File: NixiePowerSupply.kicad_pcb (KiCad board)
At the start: 2 copper layers, 50.8 x 44.4 mm, 21 parts, among them J1 BARREL_JACK, P1 CONN_01X03, P2 CONN_01X02, T1 IRF644, U1 MAX1771

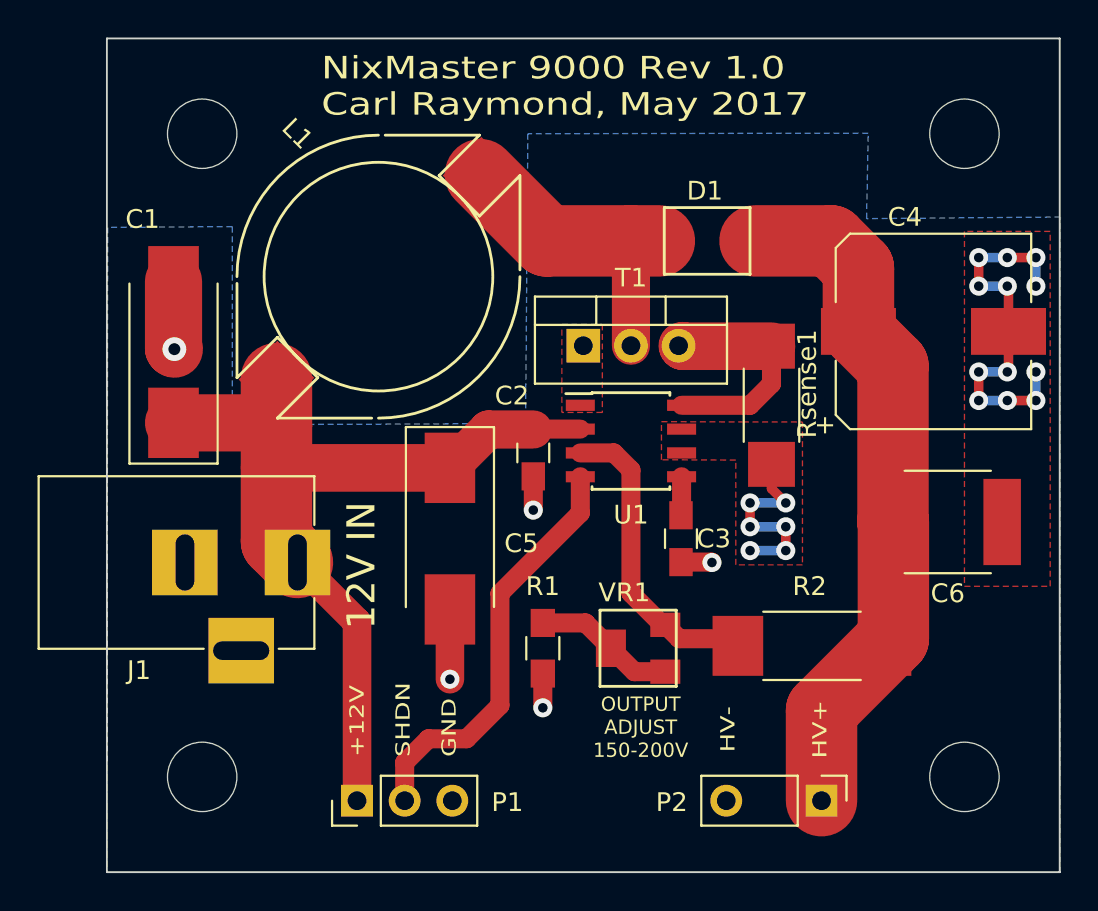
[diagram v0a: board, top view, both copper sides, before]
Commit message: Changed 12V jack to round-hole version
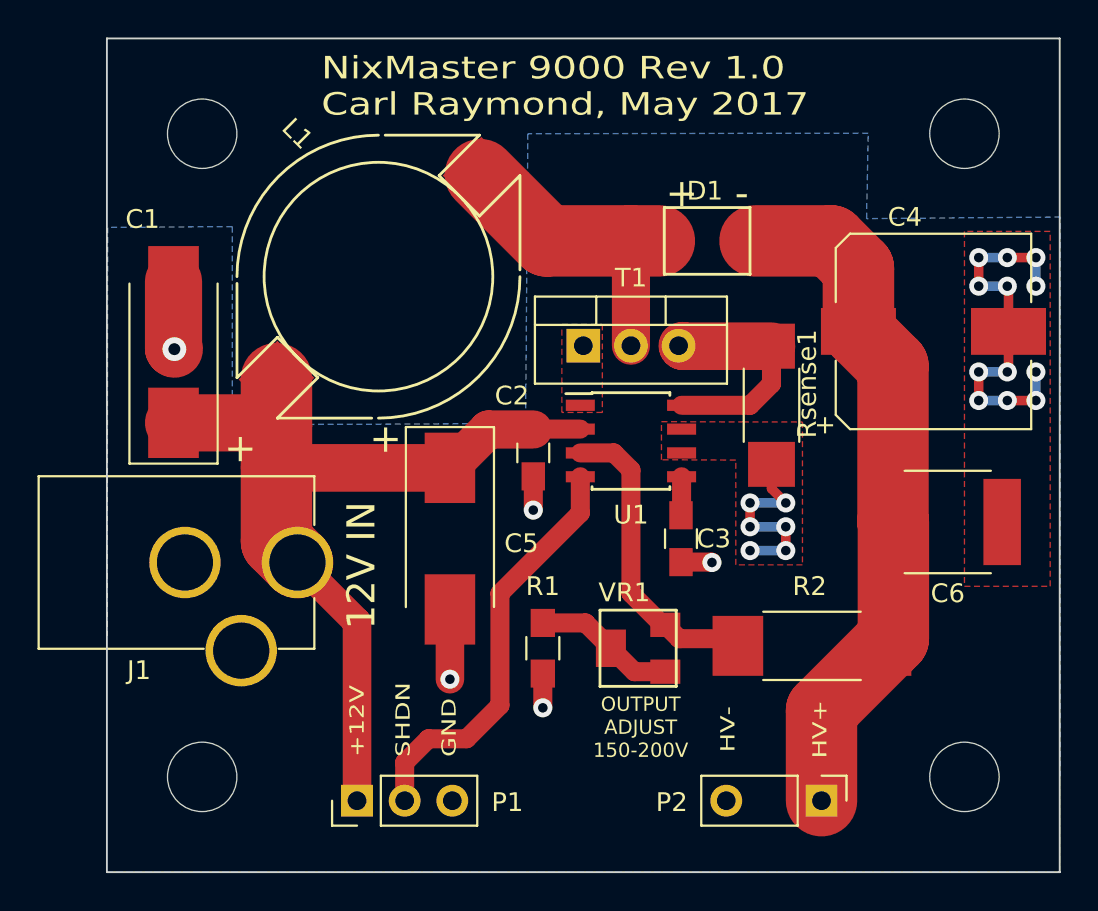
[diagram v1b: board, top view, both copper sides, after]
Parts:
- J1: footprint Connectors:BARREL_JACK -> nixie:BARREL_JACK_ROUND_HOLES
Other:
- board text added: "+"
- board text added: "+ -"
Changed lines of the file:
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@@
     (links 34)
     (no_connects 0)
-    (area 40.384999 24.805 99.568572 72.195)
+    (area 44.399999 25.349999 95.300001 69.900001)
     (thickness 1.6)
-    (drawings 9)
+    (drawings 12)
     (tracks 105)
     (zones 0)
@@
   )
   (setup
-    (last_trace_width 1.016)
+    (last_trace_width 0.25)
     (user_trace_width 0.508)
     (user_trace_width 1.016)
@@
     (visible_elements 7FFFFFFF)
     (pcbplotparams
-      (layerselection 0x010a0_00000001)
-      (usegerberextensions false)
+      (layerselection 0x010f0_80000001)
+      (usegerberextensions true)
       (excludeedgelayer true)
       (linewidth 0.100000)
@@
       (padsonsilk false)
       (subtractmaskfromsilk false)
-      (outputformat 4)
+      (outputformat 1)
       (mirror false)
       (drillshape 0)
       (scaleselection 1)
-      (outputdirectory output/))
+      (outputdirectory output/gerber/))
   )
   (net 0 "")
@@
     (add_net "Net-(T1-Pad1)")
   )
-  (module Connectors:BARREL_JACK (layer F.Cu)
-    (at 54.61 53.34)
-    (descr "DC Barrel Jack")
-    (tags "Power Jack")
-    (fp_text reference J1 (at -8.45 5.75 180) (layer F.SilkS)
-      (effects (font (size 1 1) (thickness 0.15)))
-    )
-    (fp_text value BARREL_JACK (at -6.2 -5.5) (layer F.Fab)
-      (effects (font (size 1 1) (thickness 0.15)))
-    )
-    (fp_line (start 1 -4.5) (end 1 -4.75) (layer F.CrtYd) (width 0.05))
-    (fp_line (start 1 -4.75) (end -14 -4.75) (layer F.CrtYd) (width 0.05))
-    (fp_line (start 1 -4.5) (end 1 -2) (layer F.CrtYd) (width 0.05))
-    (fp_line (start 1 -2) (end 2 -2) (layer F.CrtYd) (width 0.05))
-    (fp_line (start 2 -2) (end 2 2) (layer F.CrtYd) (width 0.05))
-    (fp_line (start 2 2) (end 1 2) (layer F.CrtYd) (width 0.05))
-    (fp_line (start 1 2) (end 1 4.75) (layer F.CrtYd) (width 0.05))
-    (fp_line (start 1 4.75) (end -1 4.75) (layer F.CrtYd) (width 0.05))
-    (fp_line (start -1 4.75) (end -1 6.75) (layer F.CrtYd) (width 0.05))
-    (fp_line (start -1 6.75) (end -5 6.75) (layer F.CrtYd) (width 0.05))
-    (fp_line (start -5 6.75) (end -5 4.75) (layer F.CrtYd) (width 0.05))
-    (fp_line (start -5 4.75) (end -14 4.75) (layer F.CrtYd) (width 0.05))
-    (fp_line (start -14 4.75) (end -14 -4.75) (layer F.CrtYd) (width 0.05))
-    (fp_line (start -5 4.6) (end -13.8 4.6) (layer F.SilkS) (width 0.12))
-    (fp_line (start -13.8 4.6) (end -13.8 -4.6) (layer F.SilkS) (width 0.12))
-    (fp_line (start 0.9 1.9) (end 0.9 4.6) (layer F.SilkS) (width 0.12))
-    (fp_line (start 0.9 4.6) (end -1 4.6) (layer F.SilkS) (width 0.12))
-    (fp_line (start -13.8 -4.6) (end 0.9 -4.6) (layer F.SilkS) (width 0.12))
-    (fp_line (start 0.9 -4.6) (end 0.9 -2) (layer F.SilkS) (width 0.12))
-    (fp_line (start -10.2 -4.5) (end -10.2 4.5) (layer F.Fab) (width 0.1))
-    (fp_line (start -13.7 -4.5) (end -13.7 4.5) (layer F.Fab) (width 0.1))
-    (fp_line (start -13.7 4.5) (end 0.8 4.5) (layer F.Fab) (width 0.1))
-    (fp_line (start 0.8 4.5) (end 0.8 -4.5) (layer F.Fab) (width 0.1))
-    (fp_line (start 0.8 -4.5) (end -13.7 -4.5) (layer F.Fab) (width 0.1))
-    (pad 1 thru_hole rect (at 0 0) (size 3.5 3.5) (drill oval 1 3) (layers *.Cu *.Mask)
-      (net 9 "Net-(C1-Pad1)"))
-    (pad 2 thru_hole rect (at -6 0) (size 3.5 3.5) (drill oval 1 3) (layers *.Cu *.Mask)
-      (net 1 GND))
-    (pad 3 thru_hole rect (at -3 4.7) (size 3.5 3.5) (drill oval 3 1) (layers *.Cu *.Mask)
-      (net 1 GND))
-    (model ${KIPRJMOD}/models/AB2_PB_2MM_JACK_PTH.wrl
-      (at (xyz -0.48 0 0))
-      (scale (xyz 0.38 0.34 0.36))
-      (rotate (xyz 0 0 90))
-    )
-  )
   (module Resistors_SMD:R_0805_HandSoldering (layer F.Cu)
     (at 67.691 57.912 270)
@@
     (pad 2 smd rect (at 2.04 0 180) (size 1.524 2.18) (layers F.Cu F.Paste F.Mask)
       (net 4 "Net-(D1-Pad2)"))
+    (model ${KIPRJMOD}/models/SMB.wrl
+      (at (xyz 0 -0.08500000000000001 0.05))
+      (scale (xyz 1 1 1))
+      (rotate (xyz 0 0 0))
+    )
   )
   (module Capacitors_SMD:CP_Elec_10x10 (layer F.Cu)
@@
     )
   )
+  (module nixie:BARREL_JACK_ROUND_HOLES (layer F.Cu)
+    (at 54.61 53.34)
+    (descr "DC Barrel Jack")
+    (tags "Power Jack")
+    (fp_text reference J1 (at -8.45 5.75 180) (layer F.SilkS)
+      (effects (font (size 1 1) (thickness 0.15)))
+    )
+    (fp_text value BARREL_JACK (at -6.2 -5.5) (layer F.Fab)
+      (effects (font (size 1 1) (thickness 0.15)))
+    )
+    (fp_line (start 1 -4.5) (end 1 -4.75) (layer F.CrtYd) (width 0.05))
+    (fp_line (start 1 -4.75) (end -14 -4.75) (layer F.CrtYd) (width 0.05))
+    (fp_line (start 1 -4.5) (end 1 -2) (layer F.CrtYd) (width 0.05))
+    (fp_line (start 1 -2) (end 2 -2) (layer F.CrtYd) (width 0.05))
+    (fp_line (start 2 -2) (end 2 2) (layer F.CrtYd) (width 0.05))
+    (fp_line (start 2 2) (end 1 2) (layer F.CrtYd) (width 0.05))
+    (fp_line (start 1 2) (end 1 4.75) (layer F.CrtYd) (width 0.05))
+    (fp_line (start 1 4.75) (end -1 4.75) (layer F.CrtYd) (width 0.05))
+    (fp_line (start -1 4.75) (end -1 6.75) (layer F.CrtYd) (width 0.05))
+    (fp_line (start -1 6.75) (end -5 6.75) (layer F.CrtYd) (width 0.05))
+    (fp_line (start -5 6.75) (end -5 4.75) (layer F.CrtYd) (width 0.05))
+    (fp_line (start -5 4.75) (end -14 4.75) (layer F.CrtYd) (width 0.05))
+    (fp_line (start -14 4.75) (end -14 -4.75) (layer F.CrtYd) (width 0.05))
+    (fp_line (start -5 4.6) (end -13.8 4.6) (layer F.SilkS) (width 0.12))
+    (fp_line (start -13.8 4.6) (end -13.8 -4.6) (layer F.SilkS) (width 0.12))
+    (fp_line (start 0.9 1.9) (end 0.9 4.6) (layer F.SilkS) (width 0.12))
+    (fp_line (start 0.9 4.6) (end -1 4.6) (layer F.SilkS) (width 0.12))
+    (fp_line (start -13.8 -4.6) (end 0.9 -4.6) (layer F.SilkS) (width 0.12))
+    (fp_line (start 0.9 -4.6) (end 0.9 -2) (layer F.SilkS) (width 0.12))
+    (fp_line (start -10.2 -4.5) (end -10.2 4.5) (layer F.Fab) (width 0.1))
+    (fp_line (start -13.7 -4.5) (end -13.7 4.5) (layer F.Fab) (width 0.1))
+    (fp_line (start -13.7 4.5) (end 0.8 4.5) (layer F.Fab) (width 0.1))
+    (fp_line (start 0.8 4.5) (end 0.8 -4.5) (layer F.Fab) (width 0.1))
+    (fp_line (start 0.8 -4.5) (end -13.7 -4.5) (layer F.Fab) (width 0.1))
+    (pad 2 thru_hole circle (at -6 0) (size 3.81 3.81) (drill 2.999994) (layers *.Cu *.Mask)
+      (net 1 GND))
+    (pad 1 thru_hole circle (at 0 0) (size 3.81 3.81) (drill 2.999994) (layers *.Cu *.Mask)
+      (net 9 "Net-(C1-Pad1)"))
+    (pad 3 thru_hole circle (at -3 4.7) (size 3.81 3.81) (drill 2.999994) (layers *.Cu *.Mask)
+      (net 1 GND))
+    (model ${KIPRJMOD}/models/AB2_PB_2MM_JACK_PTH.wrl
+      (at (xyz -0.48 0 0))
+      (scale (xyz 0.38 0.34 0.36))
+      (rotate (xyz 0 0 90))
+    )
+  )
+  (gr_text + (at 59.309 46.736) (layer F.SilkS)
+    (effects (font (size 1.5 1.5) (thickness 0.3)))
+  )
+  (gr_text + (at 51.562 47.244) (layer F.SilkS)
+    (effects (font (size 1.5 1.5) (thickness 0.3)))
+  )
+  (gr_text "+   -" (at 76.454 33.655) (layer F.SilkS)
+    (effects (font (size 1.5 1.5) (thickness 0.3)))
+  )
   (gr_text "OUTPUT\nADJUST\n150-200V" (at 72.90816 62.12332) (layer F.SilkS)
